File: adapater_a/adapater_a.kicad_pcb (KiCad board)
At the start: 4 copper layers, 53.3 x 99.8 mm, 43 parts, among them J101 Conn_01x03, J102 CN8, J103 CN9, J104 CN7, J105 CN10, J201 Conn_01x03, J202 Conn_01x06, U101 TPS5430DDA, U102 TLV2372, U301 L6226

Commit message: Realgin nucleo connection
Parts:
- moved J105 0.64 mm to (88.3, 69.5)
- moved J102 0.63 mm to (42.5, 51.7)
- moved J104 0.63 mm to (88.3, 42.5)
- moved J103 0.63 mm to (42.5, 74.5)
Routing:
- net +3V3: track 37.0 -> 38.1 mm
- net unconnected-(J102-Pin_6-Pad6): track 0.00 -> 0.78 mm

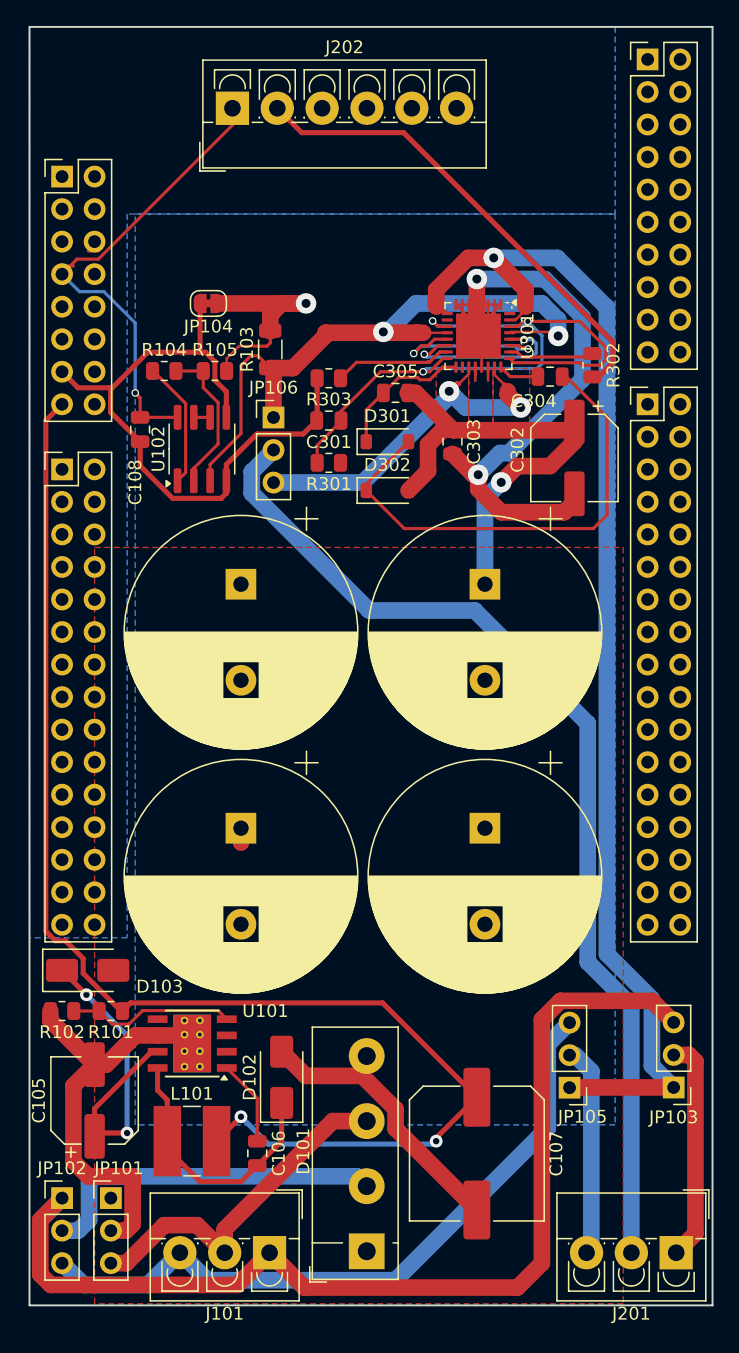
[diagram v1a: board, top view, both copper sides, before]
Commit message: Add voltage messurement
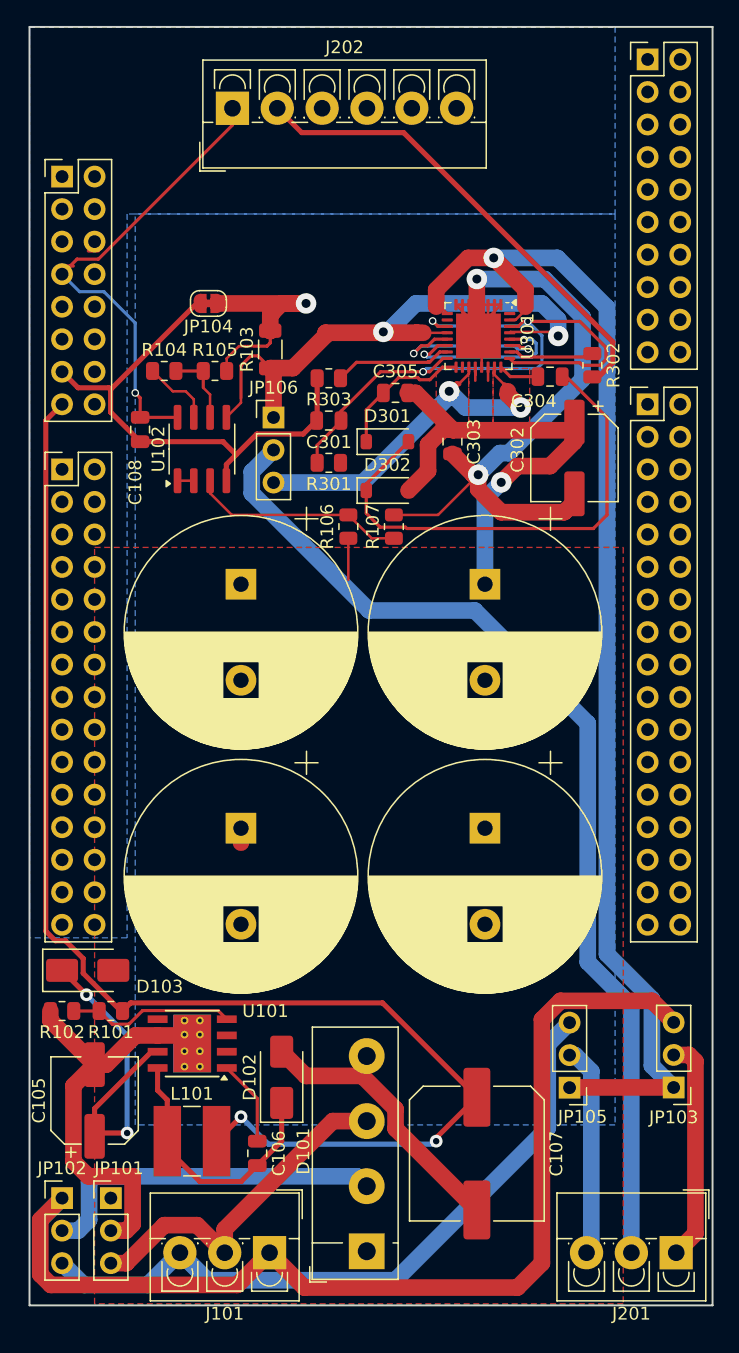
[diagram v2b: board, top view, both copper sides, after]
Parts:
- added R106: R, Resistor_SMD:R_0805_2012Metric, F.Cu at (64.9, 79.0)
- added R107: R, Resistor_SMD:R_0805_2012Metric, F.Cu at (68.4, 79.0)
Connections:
- net /Driver/V_in renamed /V_zwischenkreis
- J102 pad 10: unconnected-(J102-Pin_10-Pad10) -> /PC12
- J102 pad 12: unconnected-(J102-Pin_12-Pad12) -> /PD2
- J102 pad 14: unconnected-(J102-Pin_14-Pad14) -> /PG2
- J102 pad 16: unconnected-(J102-Pin_16-Pad16) -> /PG3
- J102 pad 2: unconnected-(J102-Pin_2-Pad2) -> /PC8
- J102 pad 4: unconnected-(J102-Pin_4-Pad4) -> /PC9
- J102 pad 6: unconnected-(J102-Pin_6-Pad6) -> /PC10
- J102 pad 8: unconnected-(J102-Pin_8-Pad8) -> /PC11
- J103 pad 10: unconnected-(J103-Pin_10-Pad10) -> /PD3
- J103 pad 11: unconnected-(J103-Pin_11-Pad11) -> /PF10
- J103 pad 12: unconnected-(J103-Pin_12-Pad12) -> GND
- J103 pad 14: unconnected-(J103-Pin_14-Pad14) -> /PE2
- J103 pad 16: unconnected-(J103-Pin_16-Pad16) -> /PE4
- J103 pad 17: unconnected-(J103-Pin_17-Pad17) -> /PF2
- J103 pad 18: unconnected-(J103-Pin_18-Pad18) -> /PE5
- J103 pad 19: unconnected-(J103-Pin_19-Pad19) -> /PF1
- J103 pad 2: unconnected-(J103-Pin_2-Pad2) -> /PD7
- J103 pad 20: unconnected-(J103-Pin_20-Pad20) -> /PE6
- J103 pad 21: unconnected-(J103-Pin_21-Pad21) -> /PF0
- J103 pad 22: unconnected-(J103-Pin_22-Pad22) -> /PE3
- J103 pad 23: unconnected-(J103-Pin_23-Pad23) -> GND
- J103 pad 24: unconnected-(J103-Pin_24-Pad24) -> /PF8
- J103 pad 25: unconnected-(J103-Pin_25-Pad25) -> /PD0
- J103 pad 26: unconnected-(J103-Pin_26-Pad26) -> /PF7
- J103 pad 27: unconnected-(J103-Pin_27-Pad27) -> /PD1
- J103 pad 28: unconnected-(J103-Pin_28-Pad28) -> /PF9
- J103 pad 29: unconnected-(J103-Pin_29-Pad29) -> /PG0
- J103 pad 30: unconnected-(J103-Pin_30-Pad30) -> /PG1
- J103 pad 4: unconnected-(J103-Pin_4-Pad4) -> /PD6
- J103 pad 6: unconnected-(J103-Pin_6-Pad6) -> /PD5
- J103 pad 8: unconnected-(J103-Pin_8-Pad8) -> /PD4
- J103 pad 9: unconnected-(J103-Pin_9-Pad9) -> /PF5
- J104 pad 1: unconnected-(J104-Pin_1-Pad1) -> /PC6
- J104 pad 10: unconnected-(J104-Pin_10-Pad10) -> /PA5
- J104 pad 11: unconnected-(J104-Pin_11-Pad11) -> /PC7
- J104 pad 12: unconnected-(J104-Pin_12-Pad12) -> /PA6
- J104 pad 13: unconnected-(J104-Pin_13-Pad13) -> /PB5
- J104 pad 14: unconnected-(J104-Pin_14-Pad14) -> /PA7
- J104 pad 15: unconnected-(J104-Pin_15-Pad15) -> /PB3
- J104 pad 16: unconnected-(J104-Pin_16-Pad16) -> /PD14
- J104 pad 17: unconnected-(J104-Pin_17-Pad17) -> /PA4
- J104 pad 18: unconnected-(J104-Pin_18-Pad18) -> /PD15
- J104 pad 19: unconnected-(J104-Pin_19-Pad19) -> /PB4
- J104 pad 2: unconnected-(J104-Pin_2-Pad2) -> /PB8
- J104 pad 20: unconnected-(J104-Pin_20-Pad20) -> /PF12
- J104 pad 3: unconnected-(J104-Pin_3-Pad3) -> /PB15
- J104 pad 4: unconnected-(J104-Pin_4-Pad4) -> /PB9
- J104 pad 5: unconnected-(J104-Pin_5-Pad5) -> /PB13
- J104 pad 6: unconnected-(J104-Pin_6-Pad6) -> VDDA
- J104 pad 7: unconnected-(J104-Pin_7-Pad7) -> /PB12
- J104 pad 8: unconnected-(J104-Pin_8-Pad8) -> GNDA
- J104 pad 9: unconnected-(J104-Pin_9-Pad9) -> /PA15
- J105 pad 1: unconnected-(J105-Pin_1-Pad1) -> VDDA
- J105 pad 10: unconnected-(J105-Pin_10-Pad10) -> /PE13
- J105 pad 11: unconnected-(J105-Pin_11-Pad11) -> /PF4
- J105 pad 12: unconnected-(J105-Pin_12-Pad12) -> /PF15
- J105 pad 13: unconnected-(J105-Pin_13-Pad13) -> /PB6
- J105 pad 14: unconnected-(J105-Pin_14-Pad14) -> /PG14
- J105 pad 15: unconnected-(J105-Pin_15-Pad15) -> /PB2
- J105 pad 16: unconnected-(J105-Pin_16-Pad16) -> /PG9
- J105 pad 17: unconnected-(J105-Pin_17-Pad17) -> GND
- J105 pad 18: unconnected-(J105-Pin_18-Pad18) -> /PE8
- J105 pad 19: unconnected-(J105-Pin_19-Pad19) -> /PD13
- J105 pad 2: unconnected-(J105-Pin_2-Pad2) -> /PF13
- J105 pad 20: unconnected-(J105-Pin_20-Pad20) -> /PE7
- J105 pad 21: unconnected-(J105-Pin_21-Pad21) -> /PD12
- J105 pad 22: unconnected-(J105-Pin_22-Pad22) -> GND
- J105 pad 23: unconnected-(J105-Pin_23-Pad23) -> /PD11
- J105 pad 24: unconnected-(J105-Pin_24-Pad24) -> /PE10
- J105 pad 25: unconnected-(J105-Pin_25-Pad25) -> /PE2
- J105 pad 26: unconnected-(J105-Pin_26-Pad26) -> /PE12
- J105 pad 27: unconnected-(J105-Pin_27-Pad27) -> GND
- J105 pad 28: unconnected-(J105-Pin_28-Pad28) -> /PE13
- J105 pad 29: unconnected-(J105-Pin_29-Pad29) -> /PA0
- J105 pad 3: unconnected-(J105-Pin_3-Pad3) -> GNDA
- J105 pad 30: unconnected-(J105-Pin_30-Pad30) -> /PE15
- J105 pad 31: unconnected-(J105-Pin_31-Pad31) -> /PB0
- J105 pad 32: unconnected-(J105-Pin_32-Pad32) -> /PB10
- J105 pad 33: unconnected-(J105-Pin_33-Pad33) -> /PE0
- J105 pad 34: unconnected-(J105-Pin_34-Pad34) -> /PB11
- J105 pad 4: unconnected-(J105-Pin_4-Pad4) -> /PE9
- J105 pad 5: unconnected-(J105-Pin_5-Pad5) -> GND
- J105 pad 6: unconnected-(J105-Pin_6-Pad6) -> /PE11
- J105 pad 7: unconnected-(J105-Pin_7-Pad7) -> /PB1
- J105 pad 8: unconnected-(J105-Pin_8-Pad8) -> /PF14
- J105 pad 9: unconnected-(J105-Pin_9-Pad9) -> /PC2
- R104 pad 2: Net-(U102A--) -> Net-(U102B--)
- R105 pad 1: Net-(U102A--) -> Net-(U102B--)
- U102 pad 1: Net-(R104-Pad1) -> Net-(U102A--)
- U102 pad 3: /Driver/GND_SENSE -> Net-(U102A-+)
- U102 pad 5: GND -> /Driver/GND_SENSE
- U102 pad 7: Net-(U102B--) -> Net-(R104-Pad1)
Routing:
- net Net-(U102A-+): track 0.00 -> 16.8 mm
- net GND: track 88.9 -> 77.3 mm
- net Net-(U102A--): track 12.0 -> 1.27 mm
- net GNDPWR: track 134.2 -> 141.9 mm
- net /Driver/GND_SENSE: track 52.4 -> 46.9 mm
- net Net-(U102B--): track 1.27 -> 5.98 mm
- net Net-(R104-Pad1): track 9.89 -> 5.54 mm
- net /V_zwischenkreis: track 41.1 -> 44.3 mm
- net unconnected-(J102-Pin_6-Pad6): track 0.78 -> 0.00 mm
- net /PC10: track 0.00 -> 0.78 mm
- net Net-(D301-A): track 38.1 -> 38.8 mm

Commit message: Update adapter A
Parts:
- added C109: 10n, Capacitor_SMD:C_0805_2012Metric, F.Cu at (48.6, 75.6)
- added C110: 10n, Capacitor_SMD:C_0805_2012Metric, F.Cu at (51.0, 62.6)
- added D104: gr, LED_SMD:LED_0805_2012Metric, F.Cu at (86.2, 120.0)
- added D105: red, LED_SMD:LED_0805_2012Metric, F.Cu at (68.7, 44.3)
- added D106: yl, LED_SMD:LED_0805_2012Metric, F.Cu at (68.7, 47.9)
- added D107: gr, LED_SMD:LED_0805_2012Metric, F.Cu at (68.7, 51.4)
- added R108: 150, Resistor_SMD:R_0805_2012Metric, F.Cu at (91.0, 114.4)
- added R109: 150, Resistor_SMD:R_0805_2012Metric, F.Cu at (59.9, 51.4)
- added R110: 150, Resistor_SMD:R_0805_2012Metric, F.Cu at (59.9, 54.3)
- added R111: 150, Resistor_SMD:R_0805_2012Metric, F.Cu at (59.9, 57.3)
- added R112: 68k, Resistor_SMD:R_0805_2012Metric, F.Cu at (48.6, 79.0)
- added R113: 68k, Resistor_SMD:R_0805_2012Metric, F.Cu at (50.9, 64.6)
- added SW101: SW_DIP_x10, Button_Switch_SMD:SW_DIP_SPSTx10_Slide_KingTek_DSHP10TS_W7.62mm_P1.27mm, F.Cu at (79.4, 49.1)
- R106: value R -> 10k
- R107: value R -> 820
- moved J202 10.2 mm to (45.8, 44.3)
- moved JP104 2.47 mm to (55.4, 59.6)
- moved R107 0.51 mm to (67.9, 79.0)
- moved R104 0.41 mm to (50.9, 66.9)
- moved C302 0.13 mm to (82.5, 73.8)
- moved D302 0.13 mm to (67.9, 76.1)
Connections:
- J102 pad 10: /PC12 -> /TRACK_MOSI
- J102 pad 12: /PD2 -> /TRACK_CS
- J102 pad 6: /PC10 -> /TRACK_CLK
- J102 pad 8: /PC11 -> /TRACK_MISO
- J103 pad 1: /PA3 -> /ADC_current
- J103 pad 3: /PC0 -> /ADC_voltage
- J105 pad 25: /PE2 -> /PE2a
- J105 pad 28: /PE13 -> /PE14
- R301 pad 1: /Driver/EN -> /PE14
- U301 pad 13: /Driver/IN1 -> /PE13
- U301 pad 14: /Driver/IN2 -> /PE9
- U301 pad 27: /Driver/IN1 -> /PE13
- U301 pad 28: /Driver/IN2 -> /PE9
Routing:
- net /PE9: track 0.00 -> 46.4 mm, vias 0 -> 3
- net /PE14: track 0.00 -> 46.0 mm
- net /PE13: track 0.00 -> 45.9 mm, vias 0 -> 3
- net GNDPWR: track 141.9 -> 104.2 mm
- net /TRACK_MOSI: track 0.00 -> 34.9 mm
- net /PC9: track 0.00 -> 34.3 mm
- net GND: track 77.3 -> 104.7 mm, vias 0 -> 3
- net /TRACK_CS: track 0.00 -> 27.4 mm
- net GNDA: track 0.00 -> 26.2 mm
- net VDDA: track 0.00 -> 24.7 mm
- net /ADC_current: track 0.00 -> 24.5 mm
- net /TRACK_CLK: track 0.00 -> 23.5 mm
- net /PG3: track 0.00 -> 21.5 mm
- net /PG2: track 0.00 -> 21.1 mm
- net /TRACK_MISO: track 0.00 -> 20.3 mm
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- added copper zone on F.Cu, net /Driver/GND_SENSE
- added copper zone on F.Cu, net /Driver/V_TRACK
- added copper zone on F.Cu, net GND
- added copper zone on F.Cu, net GNDPWR
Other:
- copper layers 4 -> 2
- board text added: "JLCJLCJLCJLC"
- board text added: "Modellbahn Adapterboard A"
- board text added: "Rev: 1"

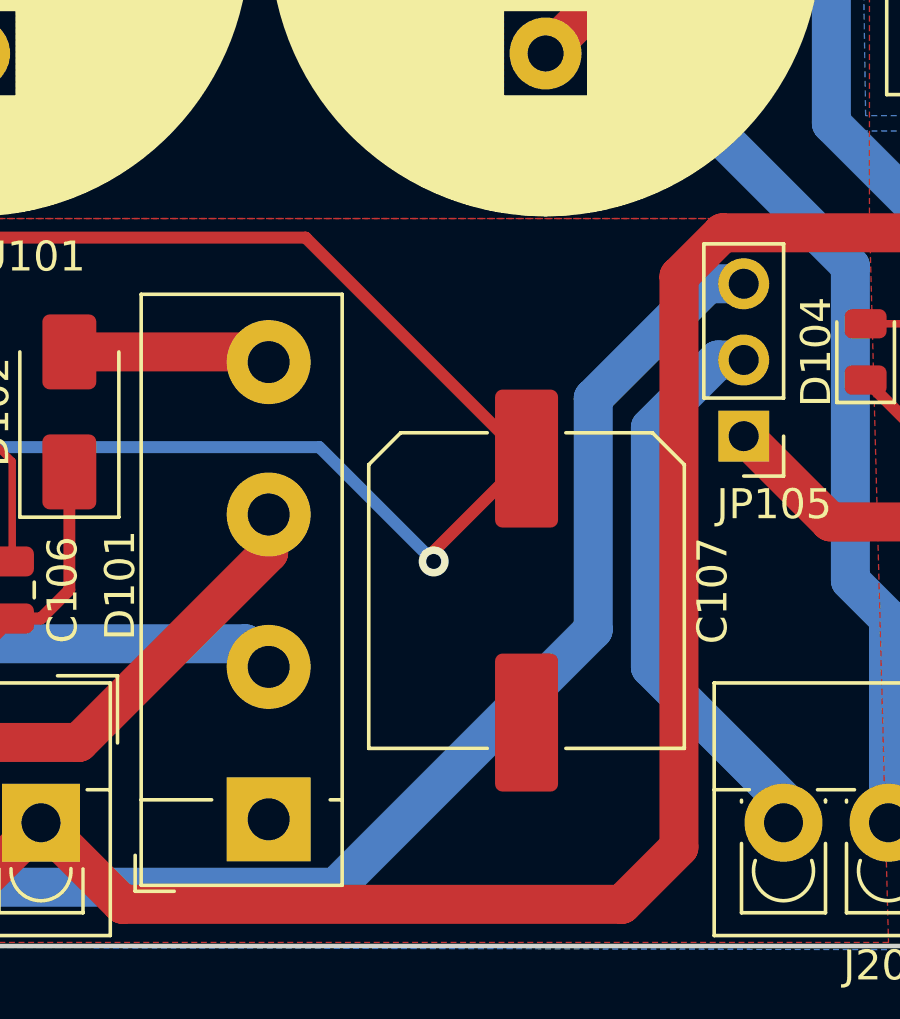
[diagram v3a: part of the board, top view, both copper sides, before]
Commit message: Add missing trace for zwischenkreis
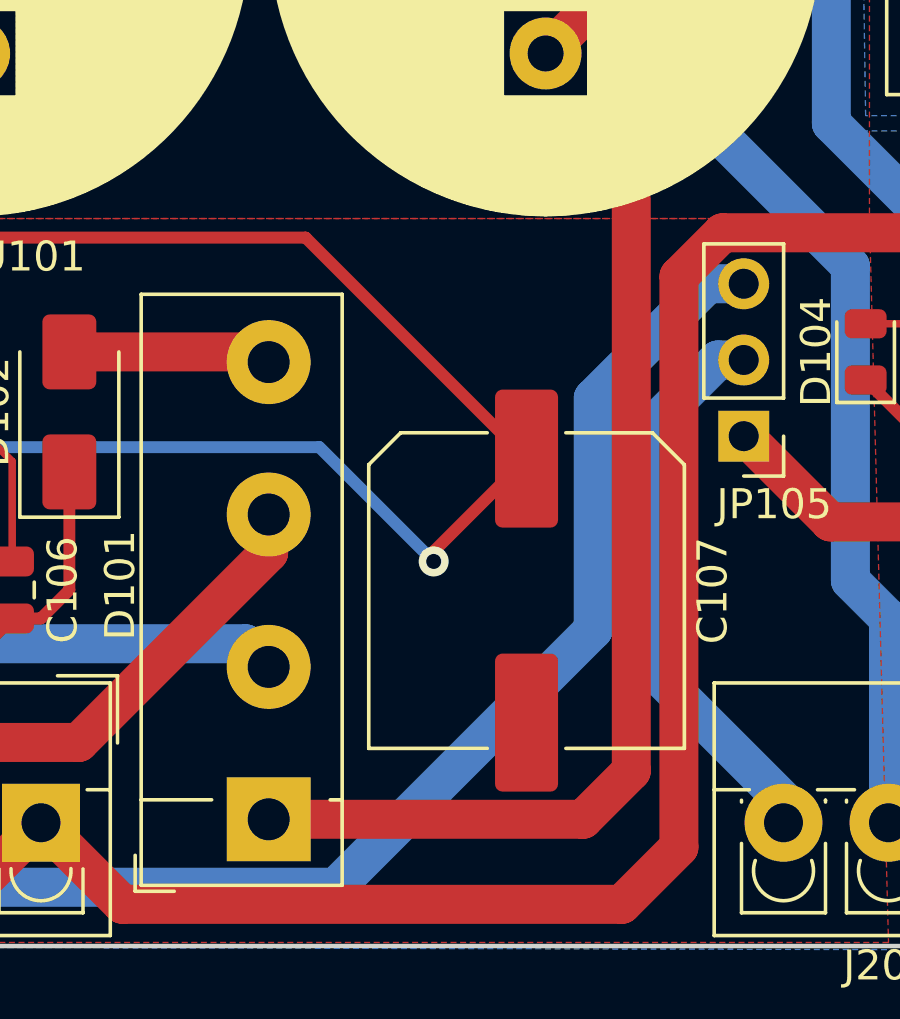
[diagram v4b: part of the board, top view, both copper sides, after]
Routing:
- net /V_zwischenkreis: track 46.2 -> 78.0 mm

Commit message: Nicer signal names
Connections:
- net /PC9 renamed /PC9_LD_red
- net /PE0 renamed /PE0_LD_gr
- net /PE13 renamed /PE13_IN1
- net /PE14 renamed /PE14_EN
- net /PE9 renamed /PE9_IN2
- net /PG2 renamed /PG2_LD_yl
- net /PG3 renamed /PG3_LD_gr
